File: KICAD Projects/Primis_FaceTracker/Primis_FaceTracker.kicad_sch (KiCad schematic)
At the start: 0 parts

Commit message: Face Tracker WIP Commit
First commit for the face tracker
-Added face tracker schematics
-Added stub for face tracker PCBs
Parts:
- added C1, C10, C4, C8, C9: 10uf, Capacitor_SMD:C_0805_2012Metric, symbol Device:C
- added C11, C12, C13, C14: 0.1uf, Capacitor_SMD:C_0603_1608Metric, symbol Device:C
- added C15: 15pF, Capacitor_SMD:C_0603_1608Metric, symbol Device:C
- added C2: 22uf, Capacitor_SMD:C_0805_2012Metric, symbol Device:C
- added C3, C7: 100nf, Capacitor_SMD:C_0603_1608Metric, symbol Device:C
- added C5: 100uf, Capacitor_SMD:C_1206_3216Metric, symbol Device:C
- added C6: 1uf, Capacitor_SMD:C_0603_1608Metric, symbol Device:C
- added CN2: KH-FG0.5-H2.0-24PIN, FaceTracker:FPC-SMD_KH-FG0.5-H2.0-24PIN, symbol kh-fg0.5-h2.0-24pin:KH-FG0.5-H2.0-24PIN
- added D1, D2, D3, D4, D5: LED, LED_SMD:LED_0805_2012Metric, symbol Device:LED
- added H1, H2, H3, H4: MountingHole, MountingHole:MountingHole_2.2mm_M2, symbol Mechanical:MountingHole
- added J1: USB_C_Receptacle_USB2.0_16P, Connector_USB:USB_C_Receptacle_HRO_TYPE-C-31-M-12, symbol Connector:USB_C_Receptacle_USB2.0_16P
- added Q1: PMOS, Package_TO_SOT_SMD:SOT-23, symbol Simulation_SPICE:PMOS
- added R1, R8: 10k, Resistor_SMD:R_0805_2012Metric, symbol Device:R
- added R10, R11, R14: 1k, Resistor_SMD:R_0805_2012Metric, symbol Device:R
- added R12, R13: 4.7k, Resistor_SMD:R_0805_2012Metric, symbol Device:R
- added R2, R3, R4, R5: 68r, Resistor_SMD:R_0603_1608Metric, symbol Device:R
- added R6, R7: 5.1k, Resistor_SMD:R_0805_2012Metric, symbol Device:R
- added R9: 100r, Resistor_SMD:R_0603_1608Metric, symbol Device:R
- added SW1, SW2: SW_SPST, Button_Switch_SMD:SW_SPST_TS-1088-xR020, symbol Switch:SW_SPST
- added U1: ESP32-S3-WROOM-1, RF_Module:ESP32-S3-WROOM-1, symbol RF_Module:ESP32-S3-WROOM-1
- added U2: AMS1117-3.3, Package_TO_SOT_SMD:SOT-223-3_TabPin2, symbol Regulator_Linear:AMS1117-3.3
- added U3: XC6206P122MR, Package_TO_SOT_SMD:SOT-23-3, symbol Regulator_Linear:XC6206PxxxMR
- added U5: XC6206P282MR, Package_TO_SOT_SMD:SOT-23-3, symbol Regulator_Linear:XC6206PxxxMR
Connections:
- new net: C8.1, Q1.1 (D), U3.3 (VI), U5.3 (VI)
- new net: R9.1, U1.27 (IO0)
- new net: R9.2, SW2.1 (A)
- new net: J1.B5 (CC2), R7.2
- new net: C6.1, C7.2, R8.1, SW1.1 (A), U1.3 (EN)
- new net: CN2.8, R14.1
- new net: D3.2 (A), R4.1
- new net: J1.A5 (CC1), R6.2
- new net: Q1.2 (G), R1.1, R10.2
- new net: D5.2 (A), R11.1
- new net: J1.A7 (D-), J1.B7 (D-), U1.13 (USB_D-)
- new net: J1.A6 (D+), J1.B6 (D+), U1.14 (USB_D+)
- new net: D4.2 (A), R5.1
- new net: D2.2 (A), R3.1
- new net: D1.2 (A), R2.1
- new net +3V3: C1.1, C13.1, C14.1, C2.1, C3.1, C5.1, CN2.11, CN2.6, Q1.3 (S), R1.2, R11.2, R12.1, R13.1, R2.2, R3.2, R4.2, R5.2, R8.2, U1.2 (3V3), U2.2 (VO)
- new net +5V: C4.1, J1.A4 (VBUS), J1.A9 (VBUS), J1.B4 (VBUS), J1.B9 (VBUS), U2.3 (VI)
- new net CAM_1.2V: C10.1, C12.1, CN2.10, U3.2 (VO)
- new net CAM_2.8V: C11.1, C9.1, CN2.4, U5.2 (VO)
- new net CAM_D0: CN2.19, U1.22 (IO14)
- new net CAM_D1: CN2.21, U1.24 (IO47)
- new net CAM_D2: CN2.22, U1.25 (IO48)
- new net CAM_D3: CN2.20, U1.23 (IO21)
- new net CAM_D4: CN2.18, U1.21 (IO13)
- new net CAM_D5: CN2.16, U1.19 (IO11)
- new net CAM_D6: CN2.14, U1.18 (IO10)
- new net CAM_D7: CN2.12, U1.17 (IO9)
- new net CAM_HSYNC: CN2.9, U1.16 (IO46)
- new net CAM_MCLK: CN2.13, U1.12 (IO8)
- new net CAM_PCLK: C15.1, CN2.17, U1.20 (IO12)
- new net CAM_PWR: R10.1
- new net CAM_SCK: CN2.5, R12.2, U1.11 (IO18)
- new net CAM_SDA: CN2.3, R13.2, U1.10 (IO17)
- new net CAM_VSYNC: CN2.7, U1.15 (IO3)
- new net GND: C1.2, C10.2, C11.2, C12.2, C13.2, C14.2, C15.2, C2.2, C3.2, C4.2, C5.2, C6.2, C7.1, C8.2, C9.2, CN2.15, CN2.2, CN2.25, CN2.26, D1.1 (K), D2.1 (K), D3.1 (K), D4.1 (K), D5.1 (K), J1.A1 (GND), J1.A12 (GND), J1.B1 (GND), J1.B12 (GND), J1.S1 (SHIELD), R14.2, R6.1, R7.1, SW1.2 (B), SW2.2 (B), U1.1 (GND), U1.40 (GND), U1.41 (GND), U2.1 (GND), U3.1 (GND), U5.1 (GND)
- no-connect marks 0 -> 3

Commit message: Face Tracker PCB
-Some work on the PCB, not quite done but I'm making some changes so uploading as a backup.
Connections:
- net D-: now reaches J1.A7 (D-), J1.B7 (D-), U1.13 (USB_D-)
- net D+: now reaches J1.A6 (D+), J1.B6 (D+), U1.14 (USB_D+)

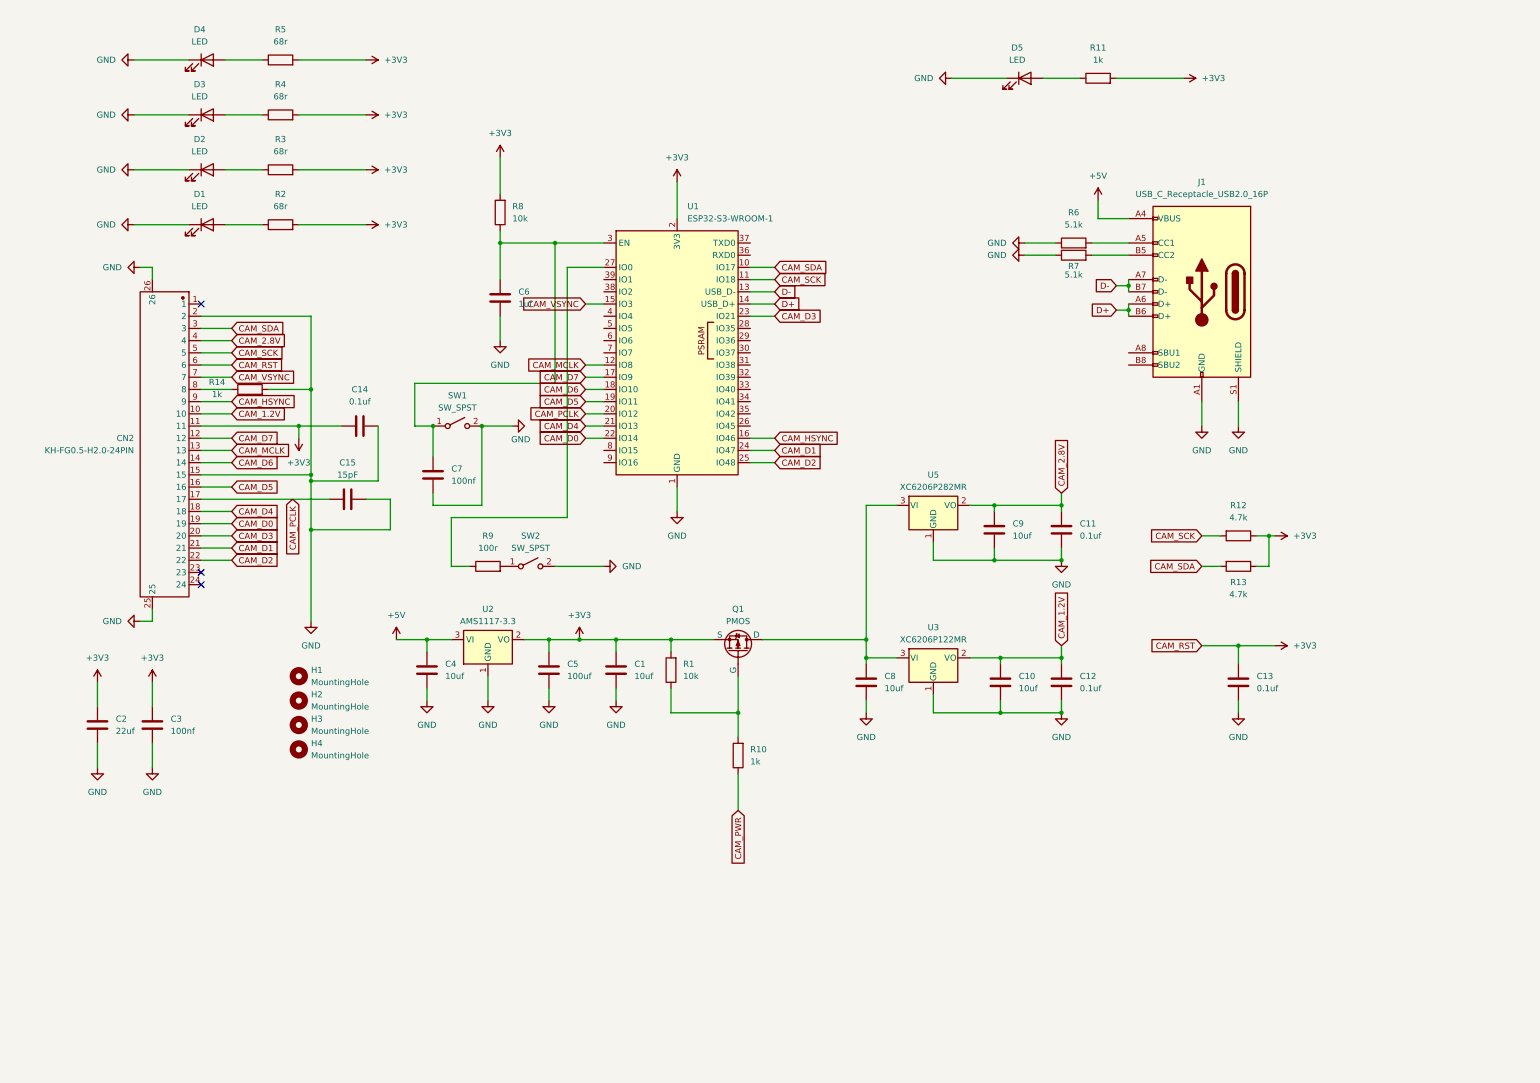
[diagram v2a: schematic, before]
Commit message: Face Tracker V1
-Roughly finished face tracker PCB
-Organised face tracker schematics
-Added face tracker images
-Added USB-C and FPC port models
-Updated README
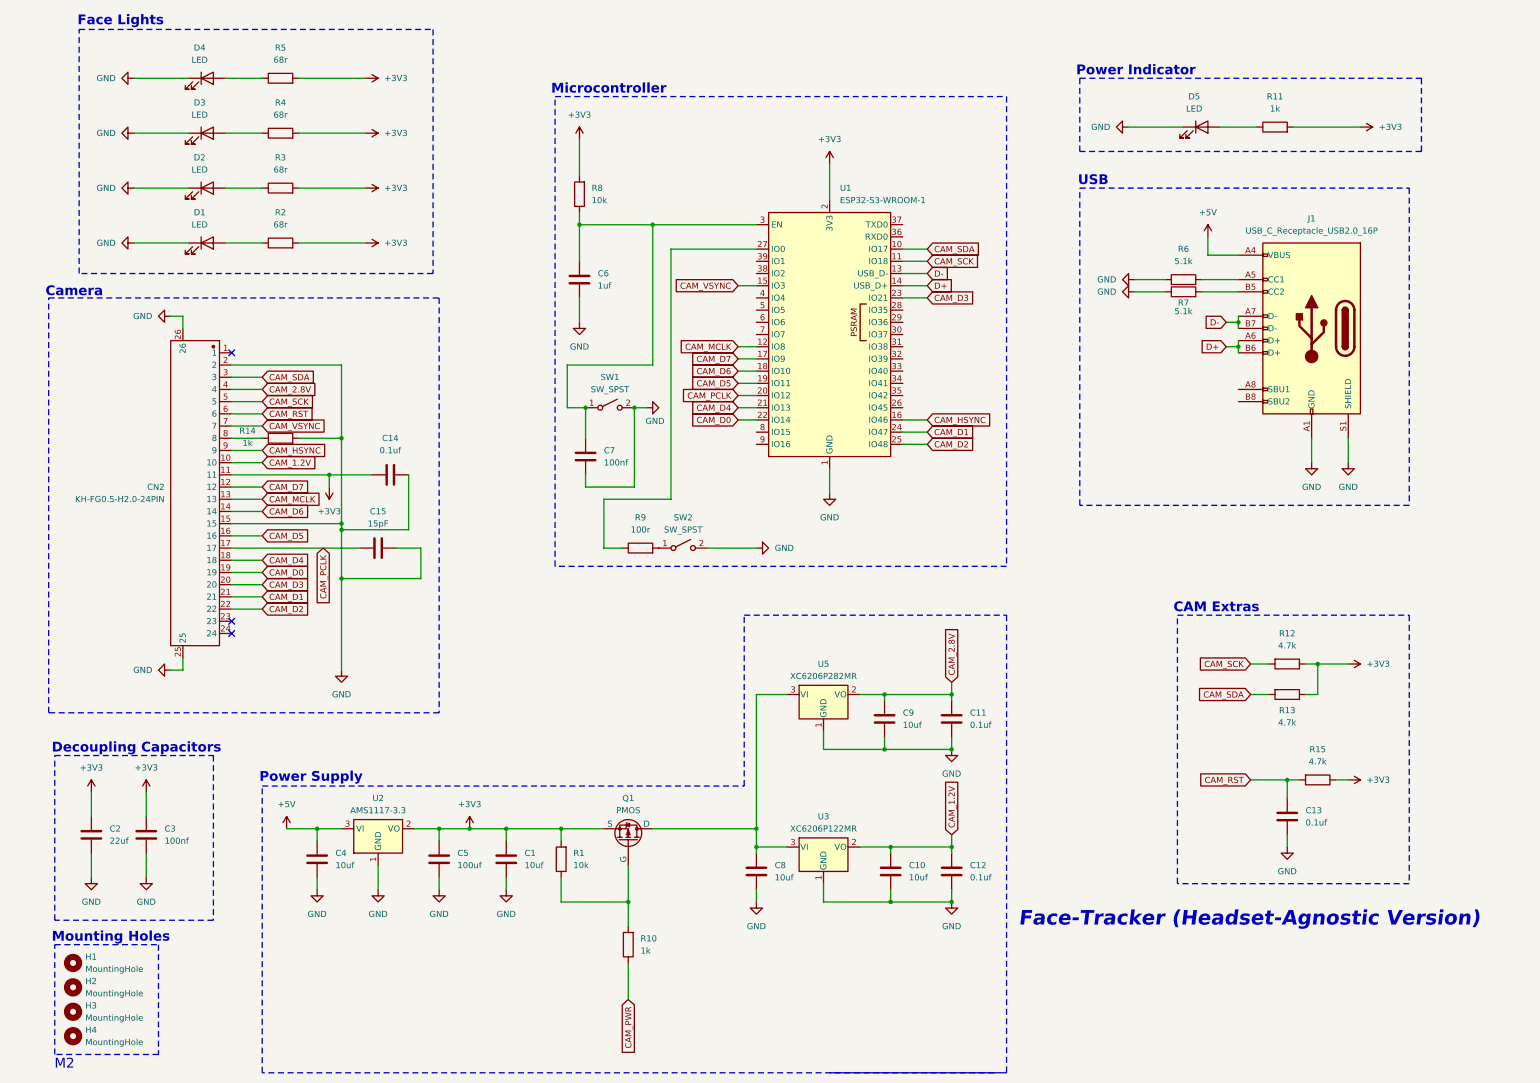
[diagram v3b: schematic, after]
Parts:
- added R15: 4.7k, Resistor_SMD:R_0805_2012Metric, symbol Device:R
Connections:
- net +3V3: now also R15.1; no longer C13.1, CN2.6
- new net CAM_RST: C13.1, CN2.6, R15.2
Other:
- note added: "CAM Extras"
- note added: "Camera"
- note added: "Decoupling Capacitors"
- note added: "Face Lights"
- note added: "Face-Tracker (Headset-Agnostic Version)"
- note added: "M2"
- note added: "Microcontroller"
- note added: "Mounting Holes"
- note added: "Power Indicator"
- note added: "Power Supply"
- note added: "USB"
- moved on the sheet: C1, C10, C11, C12, C13, C14, C15, C2, C3, C4, C5, C6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
